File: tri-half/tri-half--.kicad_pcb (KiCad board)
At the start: 2 copper layers, 50 x 43.2 mm, 8 parts, among them J1 Conn_01x05_Pin, J2 Conn_01x05_Pin, J3 Conn_01x05_Pin

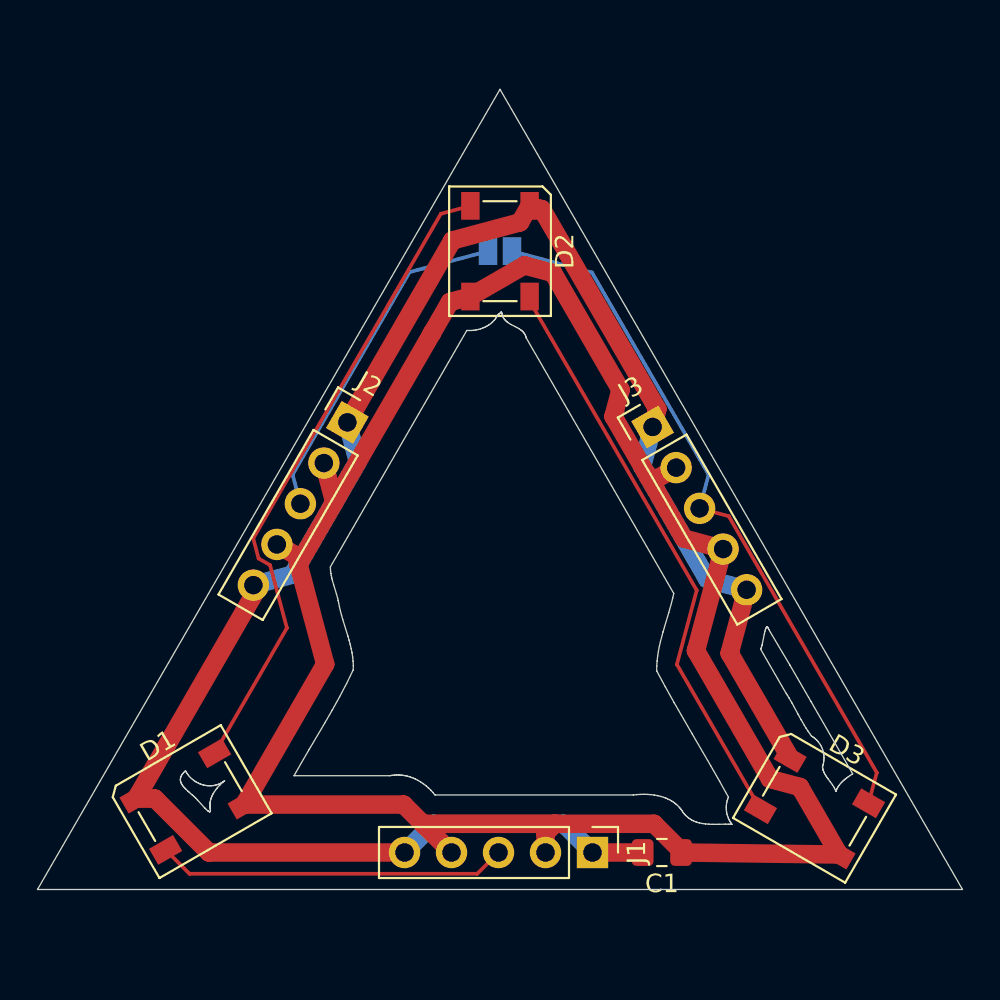
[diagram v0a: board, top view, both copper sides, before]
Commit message: added mic to antenna, decagons, octagons and all the shenanigans
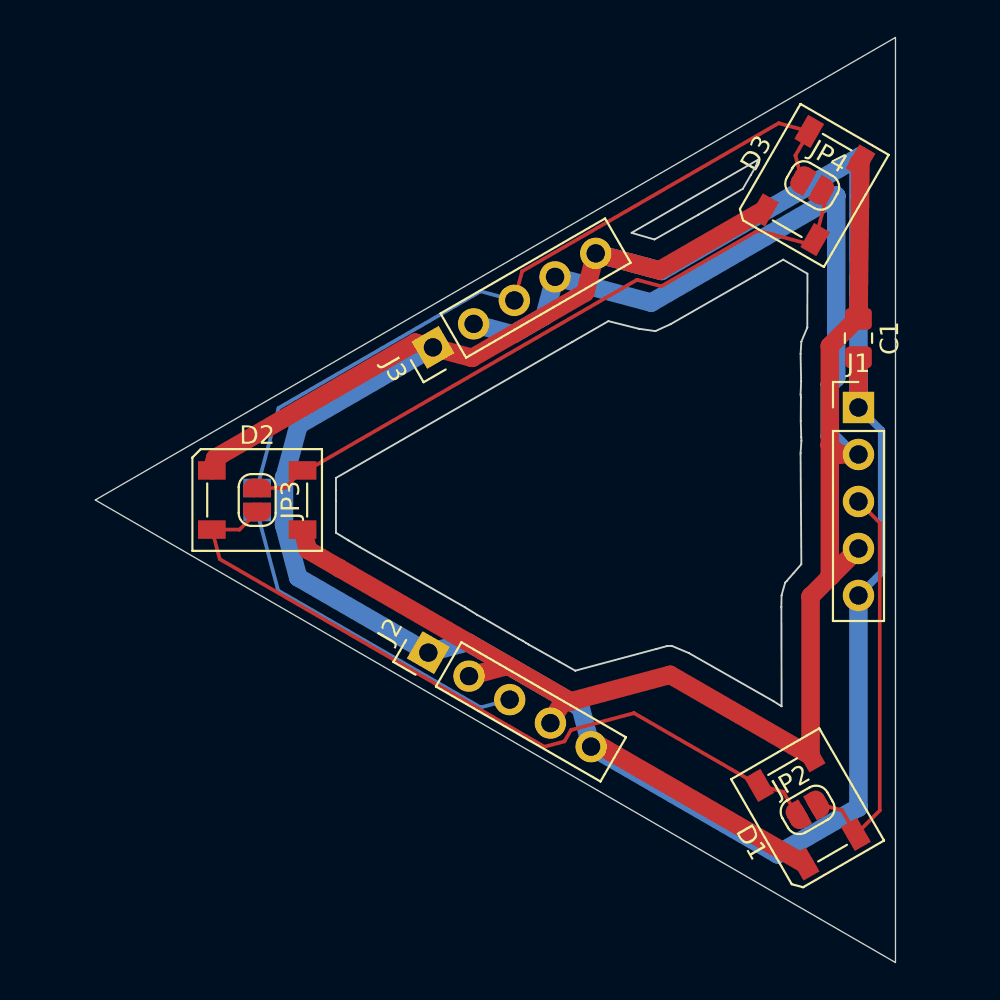
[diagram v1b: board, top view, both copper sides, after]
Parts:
- added JP2: SolderJumper_2_Open, Jumper:SolderJumper-2_P1.3mm_Open_RoundedPad1.0x1.5mm, F.Cu at (110.3, 70.9)
- added JP3: SolderJumper_2_Open, Jumper:SolderJumper-2_P1.3mm_Open_RoundedPad1.0x1.5mm, F.Cu at (80.5, 54.1)
- added JP4: SolderJumper_2_Open, Jumper:SolderJumper-2_P1.3mm_Open_RoundedPad1.0x1.5mm, F.Cu at (110.5, 37.1)
- moved D3 33.6 mm to (110.5, 37.1), turned to 60 degrees
- moved D1 33.4 mm to (110.3, 70.9), turned to 120 degrees
- moved C1 29.8 mm to (113.0, 45.4), turned to -90 degrees
- moved J1 28.0 mm to (113.0, 49.1), turned to 0 degrees
- moved JP1 18.8 mm to (80.5, 54.1), turned to 90 degrees
- moved D2 18.8 mm to (80.5, 54.1), turned to 0 degrees
- moved J2 13.2 mm to (89.8, 62.4), turned to 60 degrees
- moved J3 12.6 mm to (90.0, 45.9), turned to 120 degrees
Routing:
- net GND: track 106.5 -> 157.2 mm
- net +5V: track 118.0 -> 111.6 mm
- net Net-(D1-DOUT): track 35.1 -> 40.8 mm
- net Net-(D2-DOUT): track 31.5 -> 37.1 mm
- net Net-(D3-DOUT): track 38.3 -> 41.2 mm
- net Net-(D1-DIN): track 19.0 -> 21.8 mm
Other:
- board size 50 x 43.2 mm -> 43.3 x 50 mm
